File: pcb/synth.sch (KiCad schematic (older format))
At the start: 29 parts, among them J1 Conn_01x06, SW1 SW_Push, SW10 SW_Push, SW11 SW_Push, SW12 SW_Push, SW13 SW_Push, SW14 SW_Push, SW15 SW_Push, SW16 SW_Push, SW17 SW_Push, SW18 SW_Push, SW19 SW_Push, SW2 SW_Push, SW20 SW_Push, SW21 SW_Push, SW22 SW_Push, SW23 SW_Push, SW24 SW_Push, SW3 SW_Push, SW4 SW_Push, SW5 SW_Push, SW6 SW_Push, SW7 SW_Push, SW8 SW_Push, SW9 SW_Push, U1 STM32F407VGTx, Y1 Crystal

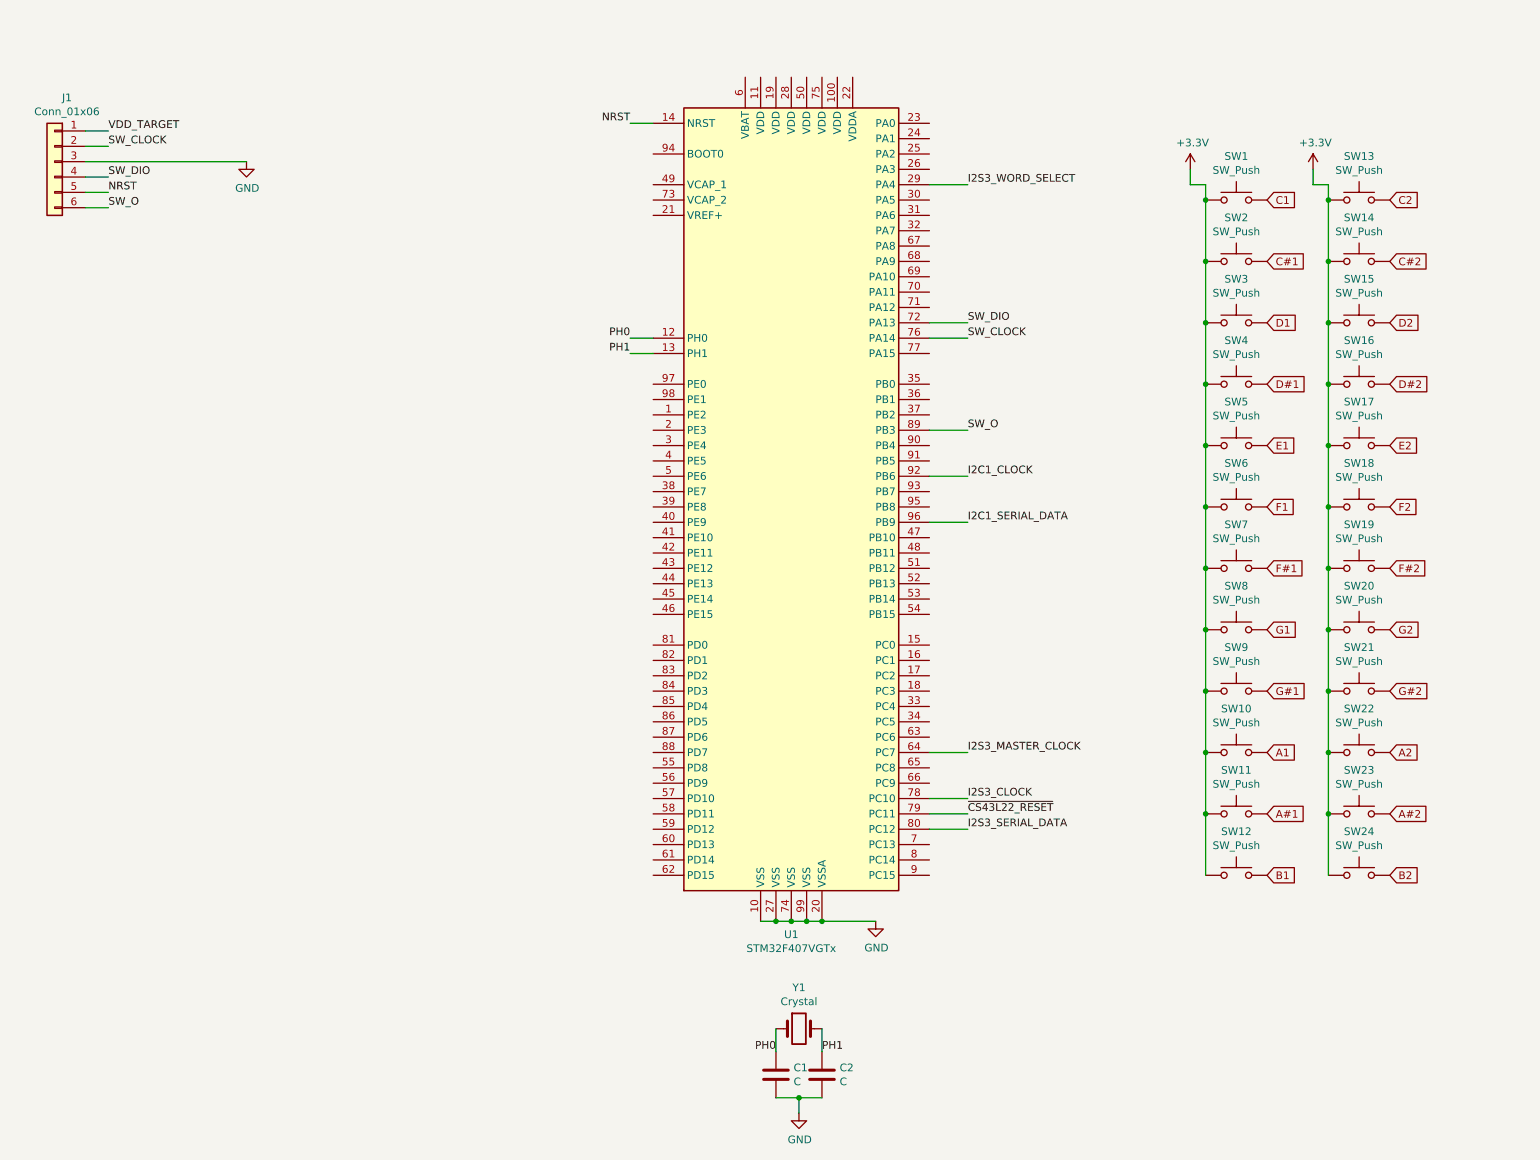
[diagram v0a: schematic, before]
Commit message: Add a bunch of decoupling caps, and populate VCAP_{1,2}.
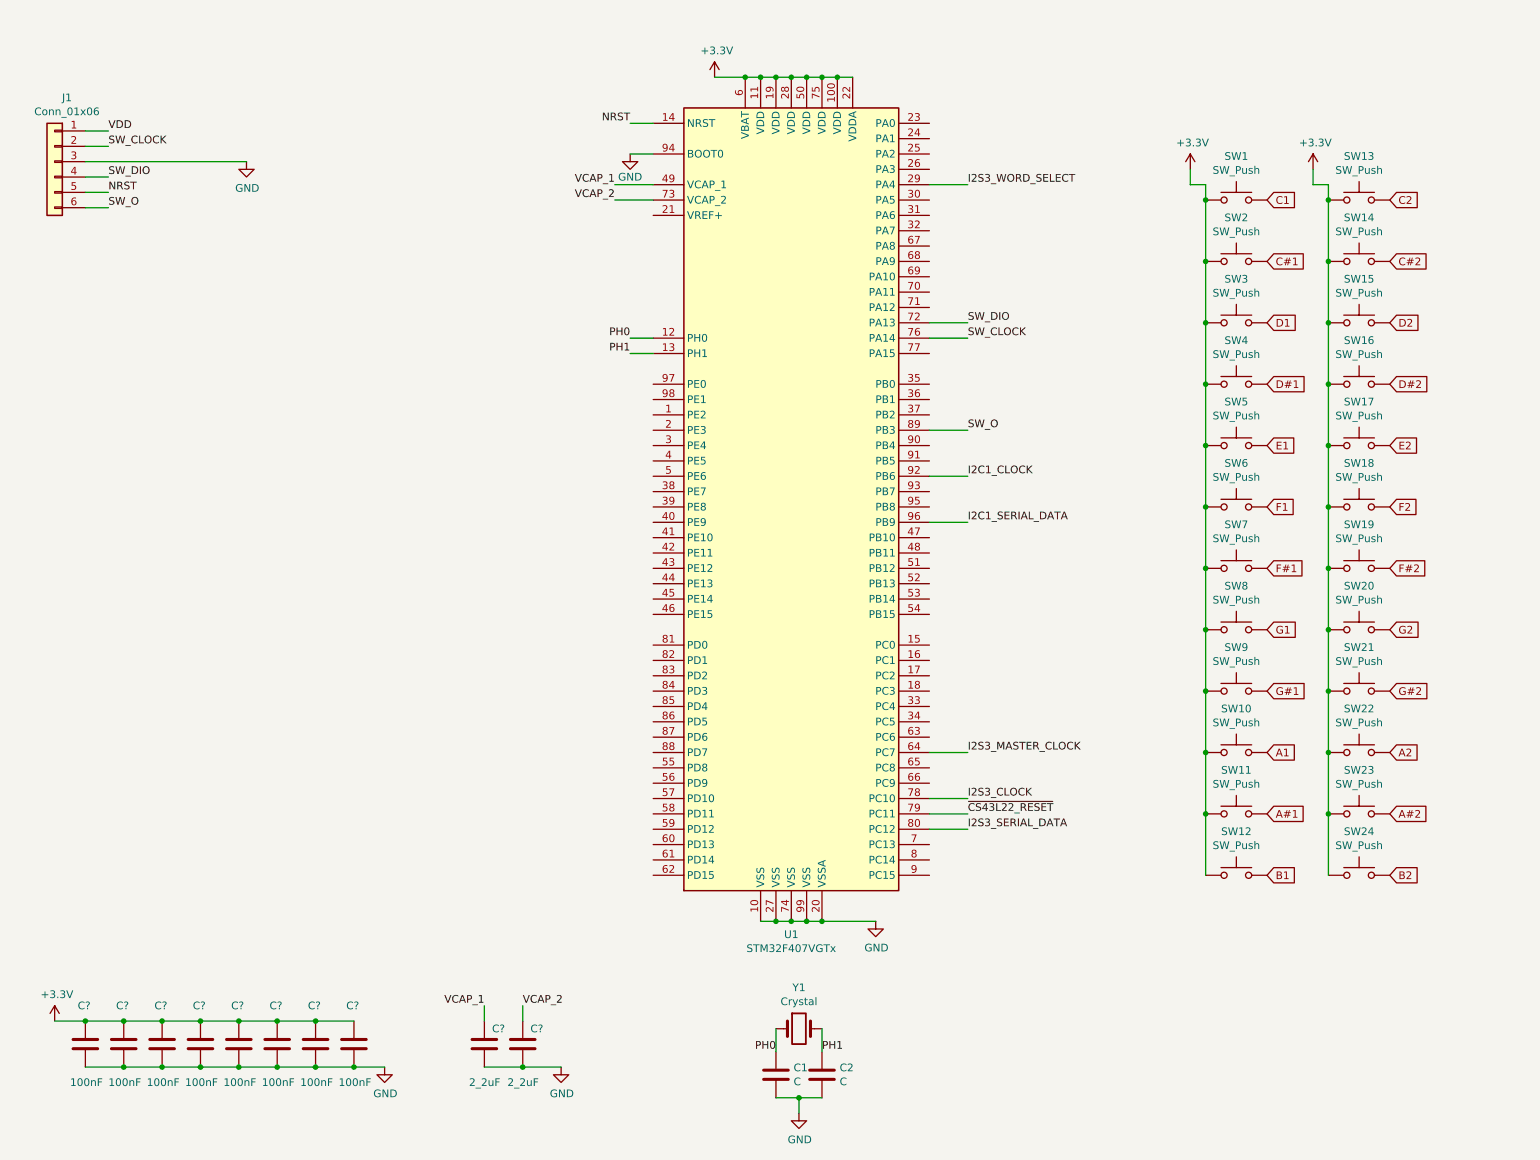
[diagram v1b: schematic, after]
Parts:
- added C? (x8): 100nF, symbol Device:C
- added C? (x2): 2_2uF, symbol Device:C
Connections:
- net +3V3: now also U1.100 (VDD), U1.11 (VDD), U1.19 (VDD), U1.22 (VDDA), U1.28 (VDD), U1.50 (VDD), U1.6 (VBAT), U1.75 (VDD), C?.1, C?.1, C?.1, C?.1, C?.1, C?.1, C?.1, C?.1
- net GND: now also U1.94 (BOOT0), C?.2, C?.2, C?.2, C?.2, C?.2, C?.2, C?.2, C?.2, C?.2, C?.2
- net VCAP_1: now reaches U1.49 (VCAP_1)
- net VCAP_1: now also C?.1
- net VCAP_2: now reaches U1.73 (VCAP_2)
- net VCAP_2: now also C?.1
- net VDD_TARGET renamed VDD

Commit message: Add a 4.7 uF cap as per page 77 of datasheet.
https://www.st.com/resource/en/datasheet/stm32f405og.pdf
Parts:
- added C?: 4_7uF, symbol Device:C
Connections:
- net +3V3: now also C?.1
- net GND: now also C?.2
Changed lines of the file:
@@
 L power:GND #PWR?
 U 1 1 5C4683D8
-P 2950 7300
-F 0 "#PWR?" H 2950 7050 50  0001 C CNN
-F 1 "GND" H 2955 7127 50  0000 C CNN
-F 2 "" H 2950 7300 50  0001 C CNN
-F 3 "" H 2950 7300 50  0001 C CNN
-	1    2950 7300
+P 3200 7300
+F 0 "#PWR?" H 3200 7050 50  0001 C CNN
+F 1 "GND" H 3205 7127 50  0000 C CNN
+F 2 "" H 3200 7300 50  0001 C CNN
+F 3 "" H 3200 7300 50  0001 C CNN
+	1    3200 7300
 	1    0    0    -1
 $EndComp
@@
 Wire Wire Line
 	2500 7300 2750 7300
+$Comp
+L Device:C C?
+U 1 1 5C46C4EB
+P 3000 7150
+F 0 "C?" H 2950 7400 50  0000 L CNN
+F 1 "4_7uF" H 2900 6900 50  0000 L CNN
+F 2 "" H 3038 7000 50  0001 C CNN
+F 3 "~" H 3000 7150 50  0001 C CNN
+	1    3000 7150
+	1    0    0    -1
+$EndComp
+Wire Wire Line
+	2750 7300 3000 7300
 Connection ~ 2750 7300
+Connection ~ 3000 7300
 Wire Wire Line
-	2750 7300 2950 7300
+	3000 7300 3200 7300
+Wire Wire Line
+	2750 7000 3000 7000
+Connection ~ 2750 7000
 $EndSCHEMATC

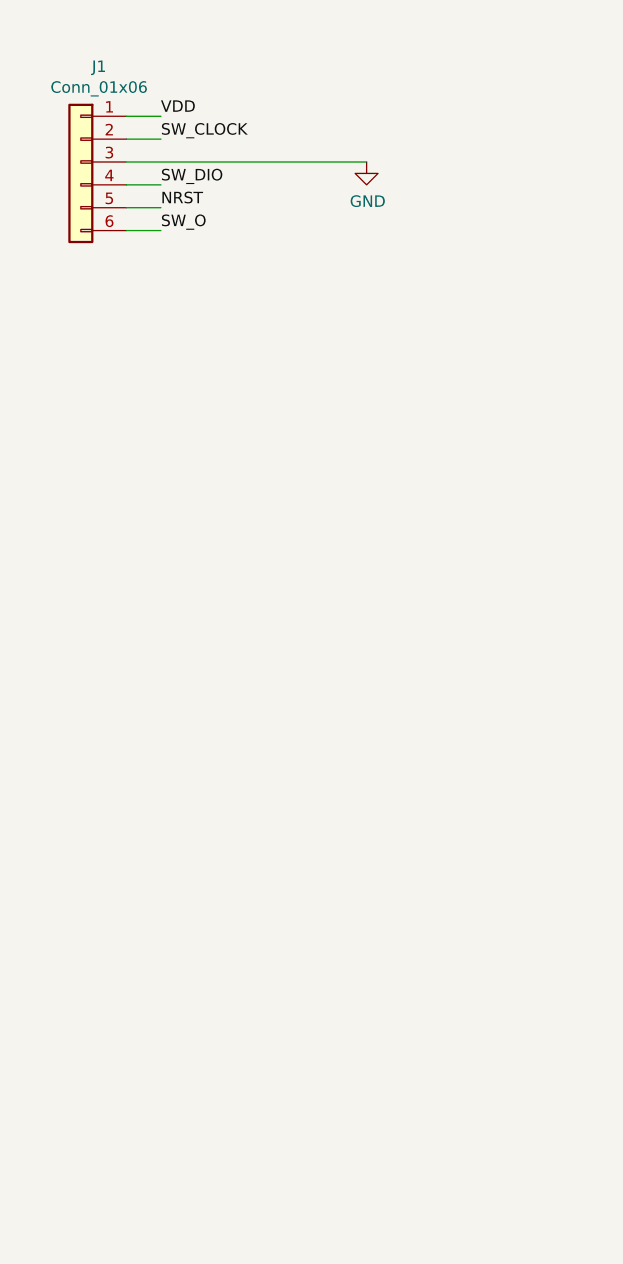
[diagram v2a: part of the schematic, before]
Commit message: Add potentiometer knobs.
This includes volume, A, D, S, R, glide speed, and mixer amount.
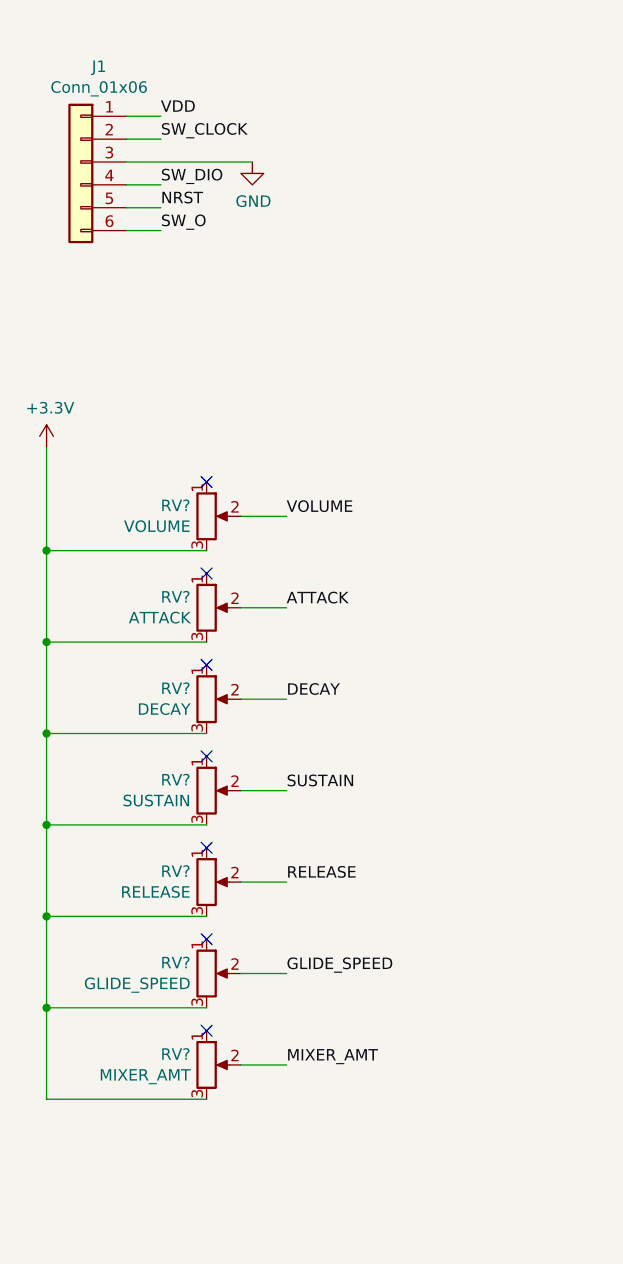
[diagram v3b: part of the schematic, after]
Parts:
- added RV?: VOLUME, symbol Device:R_POT
- added RV?: ATTACK, symbol Device:R_POT
- added RV?: DECAY, symbol Device:R_POT
- added RV?: SUSTAIN, symbol Device:R_POT
- added RV?: RELEASE, symbol Device:R_POT
- added RV?: GLIDE_SPEED, symbol Device:R_POT
- added RV?: MIXER_AMT, symbol Device:R_POT
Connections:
- net +3V3: now also RV?.3, RV?.3, RV?.3, RV?.3, RV?.3, RV?.3, RV?.3
- new net ATTACK: RV?.2
- new net DECAY: RV?.2
- new net GLIDE_SPEED: RV?.2
- new net MIXER_AMT: RV?.2
- new net RELEASE: RV?.2
- new net SUSTAIN: RV?.2
- new net VOLUME: RV?.2
- no-connect marks 0 -> 7
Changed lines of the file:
@@
 L power:GND #PWR0105
 U 1 1 5C44FBA0
-P 2050 1400
-F 0 "#PWR0105" H 2050 1150 50  0001 C CNN
-F 1 "GND" H 2055 1227 50  0000 C CNN
-F 2 "" H 2050 1400 50  0001 C CNN
-F 3 "" H 2050 1400 50  0001 C CNN
-	1    2050 1400
+P 1550 1400
+F 0 "#PWR0105" H 1550 1150 50  0001 C CNN
+F 1 "GND" H 1555 1227 50  0000 C CNN
+F 2 "" H 1550 1400 50  0001 C CNN
+F 3 "" H 1550 1400 50  0001 C CNN
+	1    1550 1400
 	1    0    0    -1
 $EndComp
@@
 Wire Wire Line
 	1000 1300 1150 1300
-Wire Wire Line
-	1000 1400 2050 1400
 Wire Wire Line
 	1000 1500 1150 1500
@@
 	2750 7000 3000 7000
 Connection ~ 2750 7000
+Wire Wire Line
+	1000 1400 1550 1400
+$Comp
+L Device:R_POT RV?
+U 1 1 5C474AFA
+P 1350 2950
+F 0 "RV?" H 1280 2996 50  0000 R CNN
+F 1 "VOLUME" H 1280 2905 50  0000 R CNN
+F 2 "" H 1350 2950 50  0001 C CNN
+F 3 "~" H 1350 2950 50  0001 C CNN
+	1    1350 2950
+	1    0    0    -1
+$EndComp
+$Comp
+L Device:R_POT RV?
+U 1 1 5C474FC1
+P 1350 3350
+F 0 "RV?" H 1280 3396 50  0000 R CNN
+F 1 "ATTACK" H 1280 3305 50  0000 R CNN
+F 2 "" H 1350 3350 50  0001 C CNN
+F 3 "~" H 1350 3350 50  0001 C CNN
+	1    1350 3350
+	1    0    0    -1
+$EndComp
+$Comp
+L Device:R_POT RV?
+U 1 1 5C4750C7
+P 1350 3750
+F 0 "RV?" H 1280 3796 50  0000 R CNN
+F 1 "DECAY" H 1280 3705 50  0000 R CNN
+F 2 "" H 1350 3750 50  0001 C CNN
+F 3 "~" H 1350 3750 50  0001 C CNN
+	1    1350 3750
+	1    0    0    -1
+$EndComp
+$Comp
+L Device:R_POT RV?
+U 1 1 5C47513D
+P 1350 4150
+F 0 "RV?" H 1280 4196 50  0000 R CNN
+F 1 "SUSTAIN" H 1280 4105 50  0000 R CNN
+F 2 "" H 1350 4150 50  0001 C CNN
+F 3 "~" H 1350 4150 50  0001 C CNN
+	1    1350 4150
+	1    0    0    -1
+$EndComp
+$Comp
+L Device:R_POT RV?
+U 1 1 5C4751B9
+P 1350 4550
+F 0 "RV?" H 1280 4596 50  0000 R CNN
+F 1 "RELEASE" H 1280 4505 50  0000 R CNN
+F 2 "" H 1350 4550 50  0001 C CNN
+F 3 "~" H 1350 4550 50  0001 C CNN
+	1    1350 4550
+	1    0    0    -1
+$EndComp
+$Comp
+L Device:R_POT RV?
+U 1 1 5C4756FF
+P 1350 4950
+F 0 "RV?" H 1280 4996 50  0000 R CNN
+F 1 "GLIDE_SPEED" H 1280 4905 50  0000 R CNN
+F 2 "" H 1350 4950 50  0001 C CNN
+F 3 "~" H 1350 4950 50  0001 C CNN
+	1    1350 4950
+	1    0    0    -1
+$EndComp
+$Comp
+L Device:R_POT RV?
+U 1 1 5C475A35
+P 1350 5350
+F 0 "RV?" H 1280 5396 50  0000 R CNN
+F 1 "MIXER_AMT" H 1280 5305 50  0000 R CNN
+F 2 "" H 1350 5350 50  0001 C CNN
+F 3 "~" H 1350 5350 50  0001 C CNN
+	1    1350 5350
+	1    0    0    -1
+$EndComp
+$Comp
+L power:+3.3V #PWR?
+U 1 1 5C478876
+P 650 2650
+F 0 "#PWR?" H 650 2500 50  0001 C CNN
+F 1 "+3.3V" H 665 2823 50  0000 C CNN
+F 2 "" H 650 2650 50  0001 C CNN
+F 3 "" H 650 2650 50  0001 C CNN
+	1    650  2650
+	1    0    0    -1
+$EndComp
+Wire Wire Line
+	650  2650 650  3100
+Wire Wire Line
+	650  5500 1350 5500
+Wire Wire Line
+	1350 5100 650  5100
+Connection ~ 650  5100
+Wire Wire Line
+	650  5100 650  5500
+Wire Wire Line
+	1350 4700 650  4700
+Connection ~ 650  4700
+Wire Wire Line
+	650  4700 650  5100
+Wire Wire Line
+	1350 4300 650  4300
+Connection ~ 650  4300
+Wire Wire Line
+	650  4300 650  4700
+Wire Wire Line
+	1350 3900 650  3900
+Connection ~ 650  3900
+Wire Wire Line
+	650  3900 650  4300
+Wire Wire Line
+	1350 3500 650  3500
+Connection ~ 650  3500
+Wire Wire Line
+	650  3500 650  3900
+Wire Wire Line
+	1350 3100 650  3100
+Connection ~ 650  3100
+Wire Wire Line
+	650  3100 650  3500
+Text Label 1700 2950 0    50   ~ 0
+VOLUME
+Text Label 1700 3350 0    50   ~ 0
+ATTACK
+Text Label 1700 3750 0    50   ~ 0
+DECAY
+Text Label 1700 4150 0    50   ~ 0
+SUSTAIN
+Text Label 1700 4550 0    50   ~ 0
+RELEASE
+Text Label 1700 4950 0    50   ~ 0
+GLIDE_SPEED
+Text Label 1700 5350 0    50   ~ 0
+MIXER_AMT
+Wire Wire Line
+	1500 2950 1700 2950
+Wire Wire Line
+	1500 3350 1700 3350
+Wire Wire Line
+	1500 3750 1700 3750
+Wire Wire Line
+	1500 4150 1700 4150
+Wire Wire Line
+	1500 4550 1700 4550
+Wire Wire Line
+	1500 4950 1700 4950
+Wire Wire Line
+	1500 5350 1700 5350
+NoConn ~ 1350 2800
+NoConn ~ 1350 3200
+NoConn ~ 1350 3600
+NoConn ~ 1350 4000
+NoConn ~ 1350 4400
+NoConn ~ 1350 4800
+NoConn ~ 1350 5200
 $EndSCHEMATC
